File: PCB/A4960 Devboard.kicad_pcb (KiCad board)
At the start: 2 copper layers, 43.4 x 48.8 mm, 58 parts, among them IC1 ATMEGA8-AI, P1 CONN_02X03, P2 CONN_01X02, P3 CONN_01X03, P4 CONN_01X03, Q1 Q_NMOS_GDS_old, Q2 Q_NMOS_GDS_old, Q3 Q_NMOS_GDS_old, Q4 Q_NMOS_GDS_old, Q5 Q_NMOS_GDS_old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

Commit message: Neue Bauteile eingefügt und angeschlossen
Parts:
- added C4: 100n, Capacitors_SMD:C_0603, F.Cu at (195.5, 101.0)
- added P5: CONN_01X03, Pin_Headers:Pin_Header_Straight_1x03, F.Cu at (223.6, 113.8)
- added P6: CONN_01X03, Pin_Headers:Pin_Header_Straight_1x03, F.Cu at (196.1, 113.8)
- added R21: 4,7k, Resistors_SMD:R_0603, F.Cu at (224.9, 111.5)
- D3: value LED -> grün
- D4: value LED -> rot
- Q1, Q2, Q3, Q4, Q5, Q6: value Q_NMOS_GDS_old -> SIRA00DP-T1-GE3
- R13: value R -> 10m
- U1: value LD1117S50TR -> AP1117D50
- moved Mount 18.9 mm to (249.3, 112.4)
- moved Mount 13.7 mm to (182.1, 113.8)
- moved R12 9.24 mm to (199.2, 107.0), turned to 90 degrees
- moved P3 1.53 mm to (205.2, 113.8)
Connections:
- C12 pad 1: +3V3 -> +5V
- C14 pad 1: +3V3 -> +5V
- IC1 pad 12: Net-(IC1-Pad12) -> (no net)
- IC1 pad 19: Net-(IC1-Pad19) -> (no net)
- IC1 pad 22: Net-(IC1-Pad22) -> (no net)
- IC1 pad 25: Net-(IC1-Pad25) -> /ADC2
- IC1 pad 26: Net-(IC1-Pad26) -> (no net)
- IC1 pad 27: Net-(IC1-Pad27) -> (no net)
- IC1 pad 28: Net-(IC1-Pad28) -> (no net)
- IC1 pad 4: +3V3 -> +5V
- IC1 pad 6: +3V3 -> +5V
- P1 pad 2: +3V3 -> +5V
- R1 pad 1: +3V3 -> +5V
- R12 pad 2: Net-(IC1-Pad1) -> Net-(IC1-Pad9)
- R2 pad 1: +3V3 -> +5V
- R9 pad 1: +3V3 -> +5V
- U1 pad 2: +3V3 -> +5V
- U2 pad 4: +3V3 -> +5V
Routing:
- net +5V: track 0.00 -> 122.4 mm, vias 0 -> 2
- net +3V3: track 109.7 -> 0.00 mm, vias 3 -> 0
- net Net-(IC1-Pad1): track 1.90 -> 45.5 mm, vias 0 -> 2
- net /ADC2: track 0.00 -> 35.8 mm, vias 0 -> 1
- net GND: track 151.9 -> 147.0 mm, vias 35 -> 34
- net Net-(IC1-Pad30): track 17.9 -> 15.4 mm
- net Net-(IC1-Pad9): track 0.00 -> 1.75 mm
- net Net-(C15-Pad2): track 8.50 -> 6.92 mm
- net /TX: track 2.82 -> 4.37 mm
- net /RX: track 2.98 -> 4.52 mm
- net Net-(R11-Pad2): track 52.0 -> 50.8 mm
- net Net-(R12-Pad1): track 51.4 -> 52.1 mm
- net /MISO: track 16.3 -> 16.8 mm, vias 0 -> 1
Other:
- board size 43.4 x 48.8 mm -> 43.4 x 47.5 mm

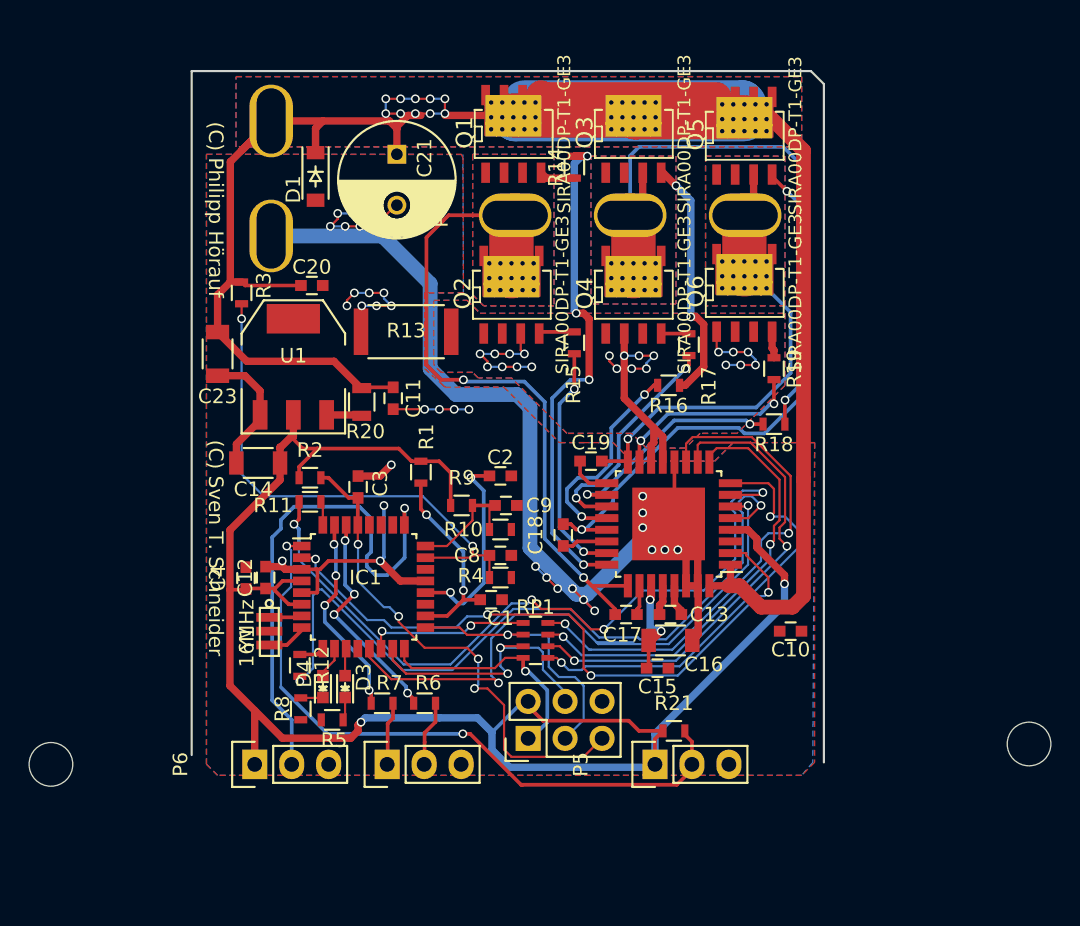
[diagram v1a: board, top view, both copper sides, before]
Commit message: Vref auf 5V gelegt und PCB fertig gelayoutet
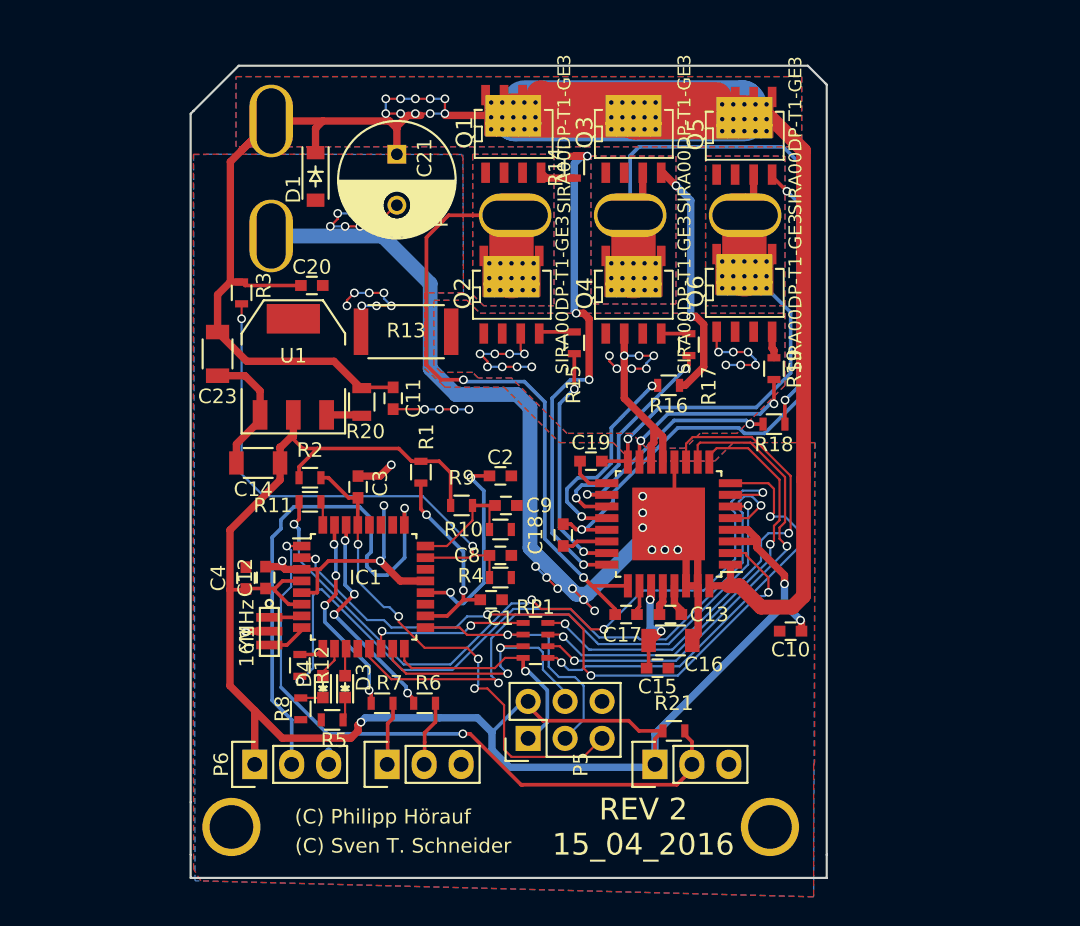
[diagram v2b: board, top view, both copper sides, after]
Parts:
- removed Mount (x2): MountingHole_3mm, Mounting_Holes:MountingHole_3mm
- added REF**: MountingHole_2.2mm_M2_DIN965_Pad, Mounting_Holes:MountingHole_2.2mm_M2_DIN965_Pad, F.Cu at (231.5, 118.1)
- added REF**: MountingHole_2.2mm_M2_DIN965_Pad, Mounting_Holes:MountingHole_2.2mm_M2_DIN965_Pad, F.Cu at (194.5, 118.1)
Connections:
- C10 pad 1: +3V3 -> +5V
- U2 pad 3: +3V3 -> +5V
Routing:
- net +5V: track 122.4 -> 128.0 mm, vias 2 -> 3
- net GND: track 147.0 -> 149.5 mm, vias 34 -> 35
- net Net-(IC1-Pad13): track 42.7 -> 40.2 mm
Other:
- board size 43.4 x 47.5 mm -> 43.7 x 55.8 mm
- net class Default: via_drill 0.4 -> 0.3
- rule via_min_size: 0.4 -> 0.6
- board text added: "REV 2 15_04_2016"
